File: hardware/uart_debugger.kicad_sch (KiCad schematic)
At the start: 3 parts, among them Q1 JSM2302, U1 CH340E UART Module

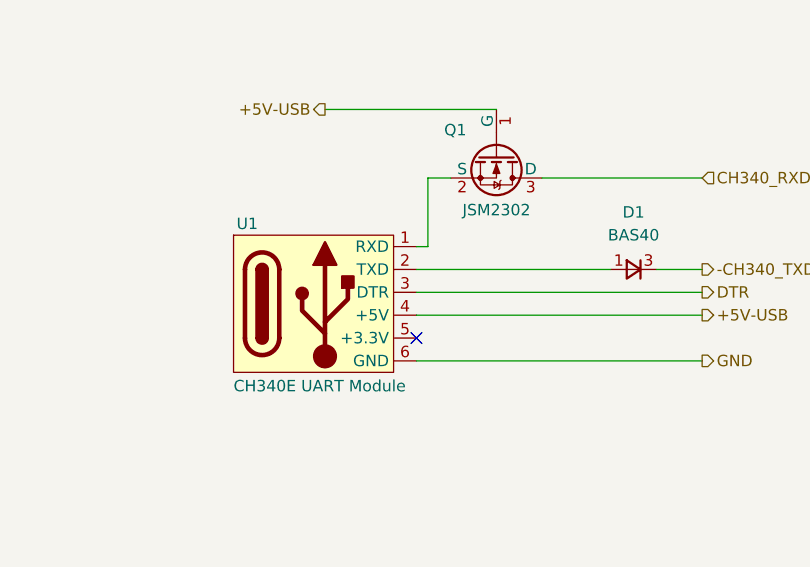
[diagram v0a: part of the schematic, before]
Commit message: I routed the display, added the SPI Test Points. Before calling it a day, I runned Rules Check and fixed all the issues related to display routing, text size and some issues with the footprints.
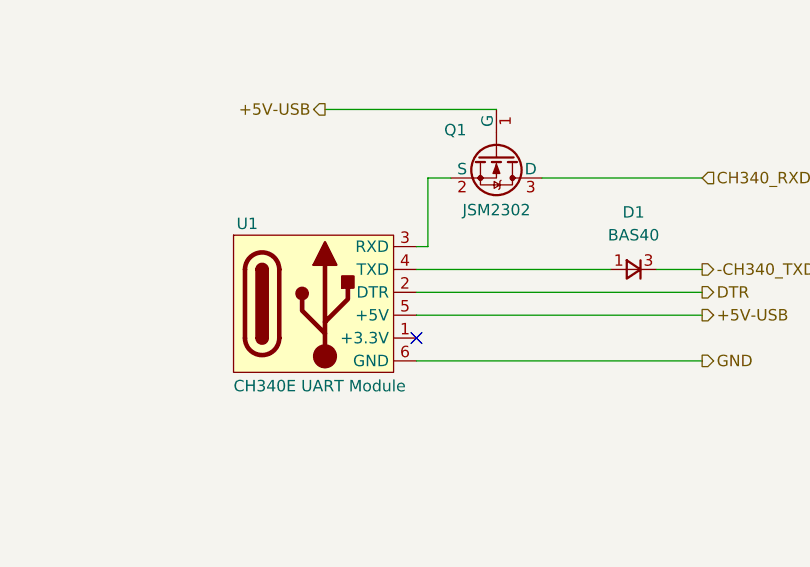
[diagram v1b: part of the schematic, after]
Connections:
- net +5V-USB: now also U1.5 (+5V); no longer U1.4 (+5V)
- net DTR: now also U1.2 (DTR); no longer U1.3 (DTR)
- net at U1.1 (+3.3V): no longer Q1.2 (S)
- net at D1.1 (A): now also U1.4 (TXD); no longer U1.2 (TXD)
- new net: Q1.2 (S), U1.3 (RXD)

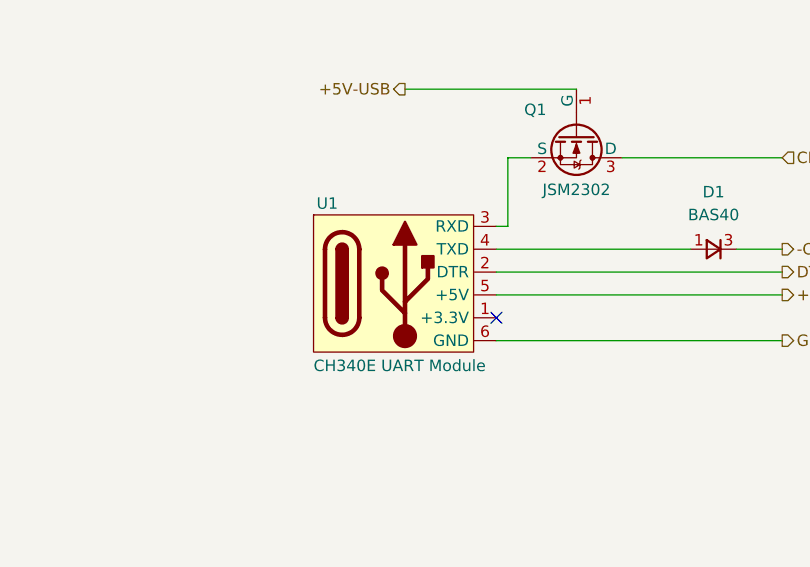
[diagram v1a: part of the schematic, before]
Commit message: Reviewed the Fields Table and marked all components that should not be populated. Then I runned rules check in the schematic and PCB
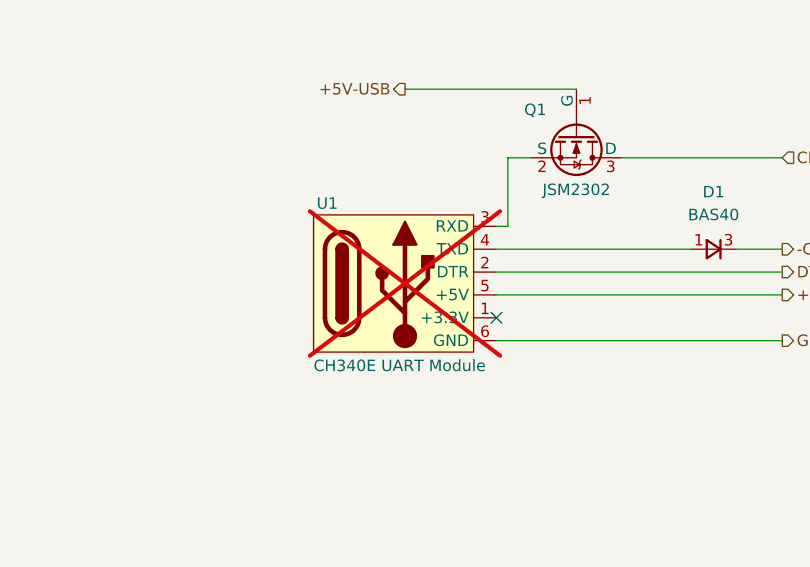
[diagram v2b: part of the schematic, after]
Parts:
- U1: now not fitted
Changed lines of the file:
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@@
 		(in_bom no)
 		(on_board yes)
-		(dnp no)
+		(dnp yes)
 		(property "Reference" "U1"
 			(at 117.094 95.25 0)

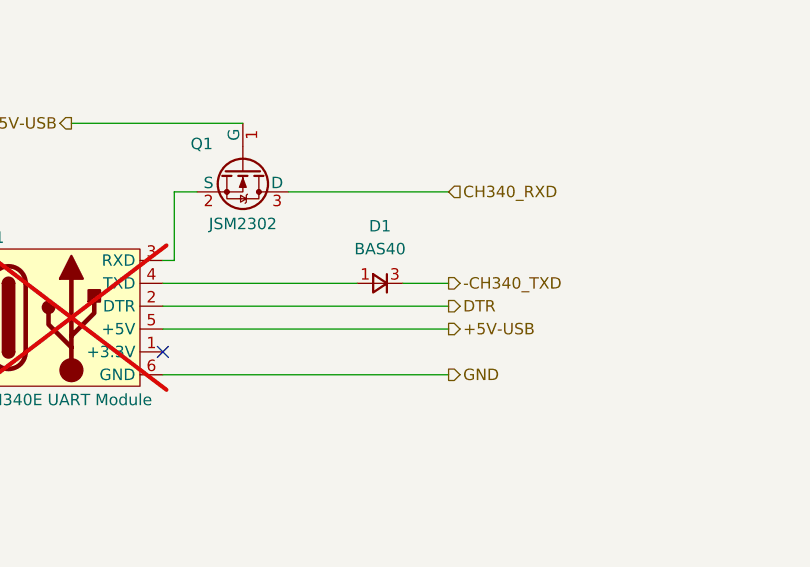
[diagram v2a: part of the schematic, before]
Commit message: Added Tx resistor, voltage devider for battery voltage mesurement.
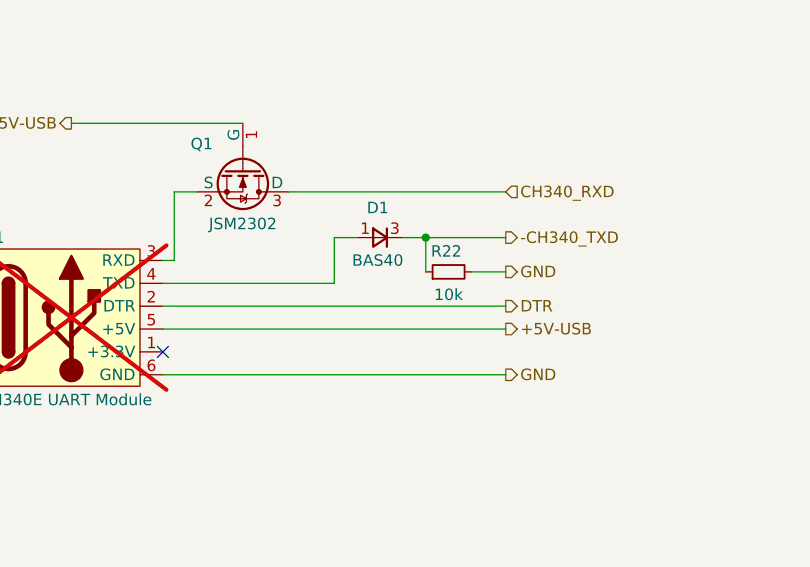
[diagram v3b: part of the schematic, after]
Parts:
- added R22: 10k, Resistor_SMD:R_0805_2012Metric_Pad1.20x1.40mm_HandSolder, symbol Device:R_Small
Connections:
- net GND: now also R22.2
- net ­CH340_TXD: now also R22.1
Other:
- moved on the sheet: D1
